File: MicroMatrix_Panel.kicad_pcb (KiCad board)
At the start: 2 copper layers, 86 x 36 mm, 321 parts

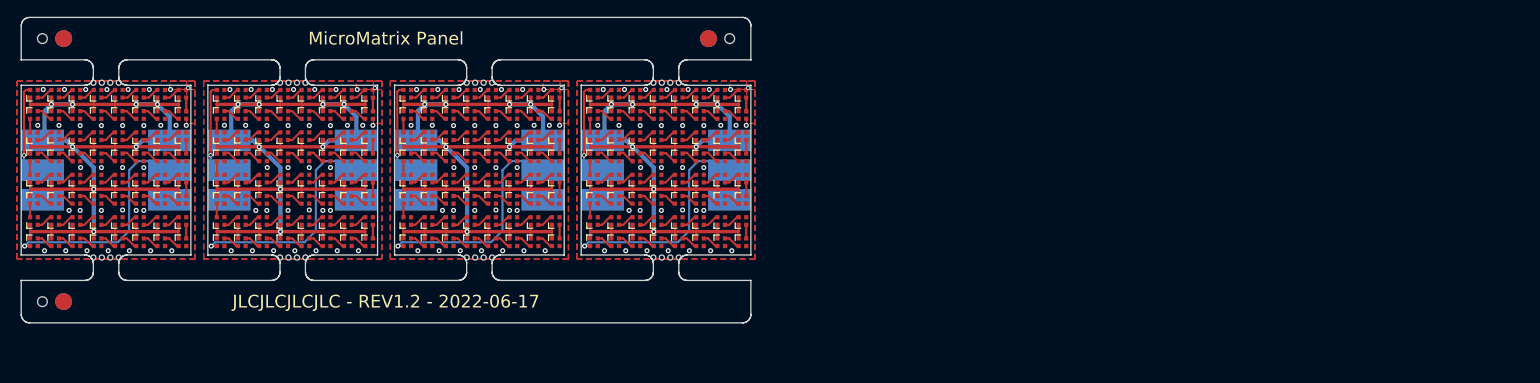
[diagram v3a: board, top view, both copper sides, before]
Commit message: Updated PCB to REV1.3 Replaced SK6805 footprint/symbol with a own version
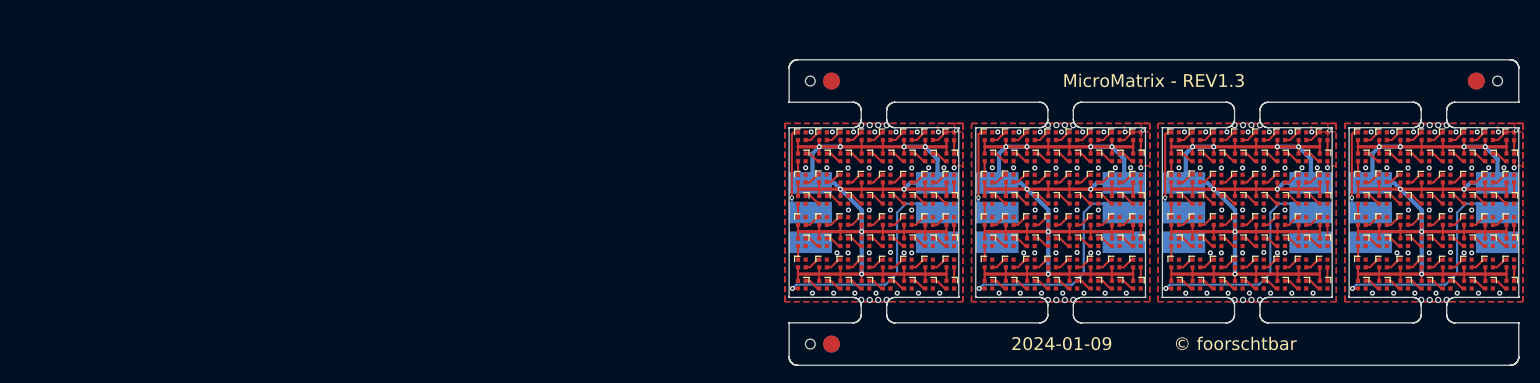
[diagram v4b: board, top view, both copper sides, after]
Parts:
- removed the ? at (39.5, 33.0)
- removed the ? at (17.5, 33.0)
- removed the ? at (83.5, 33.0)
- removed the ? at (39.5, 36.5)
- removed the ? at (76.5, 36.5)
- removed the ? at (17.5, 28.2)
- removed the ? at (17.5, 36.5)
- removed the ? at (98.5, 36.5)
- removed the ? at (98.5, 33.0)
- removed the ? at (32.5, 33.0)
- removed the ? at (61.5, 36.5)
- removed the ? at (54.5, 36.5)
- removed the ? at (54.5, 29.5)
- removed the ? at (54.5, 33.0)
- removed the ? at (83.5, 36.5)
- removed the ? at (61.5, 33.0)
- removed the ? at (98.5, 29.5)
- removed the ? at (32.5, 29.5)
- removed the ? at (61.5, 28.2)
- removed the ? at (76.5, 29.5)
- removed the ? at (39.5, 28.2)
- removed the ? at (76.5, 33.0)
- removed the ? at (83.5, 28.2)
- removed the ? at (32.5, 36.5)
- removed the D1 at (60.5, 24.0)
- removed the D1 at (16.5, 24.0)
- removed the D1 at (82.5, 24.0)
- removed the D1 at (38.5, 24.0)
- removed the D10 at (53.5, 26.5)
- removed the D10 at (31.5, 26.5)
- removed the D10 at (75.5, 26.5)
- removed the D10 at (97.5, 26.5)
- removed the D11 at (29.0, 26.5)
- removed the D11 at (73.0, 26.5)
- removed the D11 at (51.0, 26.5)
- removed the D11 at (95.0, 26.5)
- removed the D12 at (70.5, 26.5)
- removed the D12 at (92.5, 26.5)
- removed the D12 at (48.5, 26.5)
- removed the D12 at (26.5, 26.5)
- removed the D13 at (46.0, 26.5)
- removed the D13 at (24.0, 26.5)
- removed the D13 at (68.0, 26.5)
- removed the D13 at (90.0, 26.5)
- removed the D14 at (87.5, 26.5)
- removed the D14 at (43.5, 26.5)
- removed the D14 at (65.5, 26.5)
- removed the D14 at (21.5, 26.5)
- removed the D15 at (63.0, 26.5)
- removed the D15 at (19.0, 26.5)
- removed the D15 at (85.0, 26.5)
- removed the D15 at (41.0, 26.5)
- removed the D16 at (60.5, 26.5)
- removed the D16 at (82.5, 26.5)
- removed the D16 at (38.5, 26.5)
- removed the D16 at (16.5, 26.5)
- removed the D17 at (60.5, 29.0)
- removed the D17 at (16.5, 29.0)
- removed the D17 at (38.5, 29.0)
- removed the D17 at (82.5, 29.0)
- removed the D18 at (41.0, 28.9)
- removed the D18 at (63.0, 28.9)
- removed the D18 at (85.0, 28.9)
- removed the D18 at (19.0, 28.9)
- removed the D19 at (87.5, 29.0)
- removed the D19 at (43.5, 29.0)
- removed the D19 at (65.5, 29.0)
- removed the D19 at (21.5, 29.0)
- removed the D2 at (63.0, 24.0)
- removed the D2 at (85.0, 24.0)
- removed the D2 at (41.0, 24.0)
- removed the D2 at (19.0, 24.0)
- removed the D20 at (24.0, 29.0)
- removed the D20 at (46.0, 29.0)
- removed the D20 at (90.0, 29.0)
- removed the D20 at (68.0, 29.0)
- removed the D21 at (70.5, 29.0)
- removed the D21 at (48.5, 29.0)
- removed the D21 at (92.5, 29.0)
- removed the D21 at (26.5, 29.0)
- removed the D22 at (95.0, 29.0)
- removed the D22 at (29.0, 29.0)
- removed the D22 at (51.0, 29.0)
- removed the D22 at (73.0, 29.0)
- removed the D23 at (31.5, 29.0)
- removed the D23 at (53.5, 29.0)
- removed the D23 at (97.5, 29.0)
- removed the D23 at (75.5, 29.0)
- removed the D24 at (34.0, 29.0)
- removed the D24 at (56.0, 29.0)
- removed the D24 at (78.0, 29.0)
- removed the D24 at (100.0, 29.0)
- removed the D25 at (56.0, 31.5)
- removed the D25 at (78.0, 31.5)
- removed the D25 at (34.0, 31.5)
- removed the D25 at (100.0, 31.5)
- removed the D26 at (97.5, 31.5)
- removed the D26 at (75.5, 31.5)
- removed the D26 at (31.5, 31.5)
- removed the D26 at (53.5, 31.5)
- removed the D27 at (29.0, 31.5)
- removed the D27 at (73.0, 31.5)
- removed the D27 at (51.0, 31.5)
- removed the D27 at (95.0, 31.5)
- removed the D28 at (92.5, 31.5)
- removed the D28 at (70.5, 31.5)
- removed the D28 at (26.5, 31.5)
- removed the D28 at (48.5, 31.5)
- removed the D29 at (46.0, 31.5)
- removed the D29 at (90.0, 31.5)
- removed the D29 at (68.0, 31.5)
- removed the D29 at (24.0, 31.5)
- removed the D3 at (87.5, 24.0)
- removed the D3 at (43.5, 24.0)
- removed the D3 at (21.5, 24.0)
- removed the D3 at (65.5, 24.0)
- removed the D30 at (87.5, 31.5)
- removed the D30 at (65.5, 31.5)
- removed the D30 at (21.5, 31.5)
- removed the D30 at (43.5, 31.5)
- removed the D31 at (63.0, 31.5)
- removed the D31 at (85.0, 31.5)
- removed the D31 at (41.0, 31.5)
- removed the D31 at (19.0, 31.5)
- removed the D32 at (60.5, 31.5)
- removed the D32 at (38.5, 31.5)
- removed the D32 at (16.5, 31.5)
- removed the D32 at (82.5, 31.5)
- removed the D33 at (38.5, 34.0)
- removed the D33 at (82.5, 34.0)
- removed the D33 at (16.5, 34.0)
- removed the D33 at (60.5, 34.0)
- removed the D34 at (85.0, 34.0)
- removed the D34 at (19.0, 34.0)
- removed the D34 at (63.0, 34.0)
- removed the D34 at (41.0, 34.0)
- removed the D35 at (21.5, 34.0)
- removed the D35 at (43.5, 34.0)
- removed the D35 at (65.5, 34.0)
- removed the D35 at (87.5, 34.0)
- removed the D36 at (68.0, 34.0)
- removed the D36 at (46.0, 34.0)
- removed the D36 at (90.0, 34.0)
- removed the D36 at (24.0, 34.0)
- removed the D37 at (70.5, 34.0)
- removed the D37 at (92.5, 34.0)
- removed the D37 at (26.5, 34.0)
- removed the D37 at (48.5, 34.0)
- removed the D38 at (73.0, 34.0)
- removed the D38 at (95.0, 34.0)
- removed the D38 at (29.0, 34.0)
- removed the D38 at (51.0, 34.0)
- removed the D39 at (75.5, 34.0)
- removed the D39 at (31.5, 34.0)
- removed the D39 at (53.5, 34.0)
- removed the D39 at (97.5, 34.0)
- removed the D4 at (68.0, 24.0)
- removed the D4 at (90.0, 24.0)
- removed the D4 at (24.0, 24.0)
- removed the D4 at (46.0, 24.0)
- removed the D40 at (78.0, 34.0)
- removed the D40 at (34.0, 34.0)
- removed the D40 at (100.0, 34.0)
- removed the D40 at (56.0, 34.0)
- removed the D41 at (78.0, 36.5)
- removed the D41 at (100.0, 36.5)
- removed the D41 at (56.0, 36.5)
- removed the D41 at (34.0, 36.5)
- removed the D42 at (75.5, 36.5)
- removed the D42 at (97.5, 36.5)
- removed the D42 at (31.5, 36.5)
- removed the D42 at (53.5, 36.5)
- removed the D43 at (73.0, 36.5)
- removed the D43 at (29.0, 36.5)
- removed the D43 at (95.0, 36.5)
- removed the D43 at (51.0, 36.5)
- removed the D44 at (26.5, 36.5)
- removed the D44 at (92.5, 36.5)
- removed the D44 at (70.5, 36.5)
- removed the D44 at (48.5, 36.5)
- removed the D45 at (46.0, 36.5)
- removed the D45 at (68.0, 36.5)
- removed the D45 at (90.0, 36.5)
- removed the D45 at (24.0, 36.5)
- removed the D46 at (65.5, 36.5)
- removed the D46 at (43.5, 36.5)
- removed the D46 at (87.5, 36.5)
- removed the D46 at (21.5, 36.5)
- removed the D47 at (63.0, 36.5)
- removed the D47 at (19.0, 36.5)
- removed the D47 at (41.0, 36.5)
- removed the D47 at (85.0, 36.5)
- removed the D48 at (16.5, 36.5)
- removed the D48 at (38.5, 36.5)
- removed the D48 at (60.5, 36.5)
- removed the D48 at (82.5, 36.5)
- removed the D49 at (38.5, 39.0)
- removed the D49 at (16.5, 39.0)
- removed the D49 at (82.5, 39.0)
- removed the D49 at (60.5, 39.0)
- removed the D5 at (70.5, 24.0)
- removed the D5 at (26.5, 24.0)
- removed the D5 at (48.5, 24.0)
- removed the D5 at (92.5, 24.0)
- removed the D50 at (63.0, 39.0)
- removed the D50 at (19.0, 39.0)
- removed the D50 at (85.0, 39.0)
- removed the D50 at (41.0, 39.0)
- removed the D51 at (21.5, 39.0)
- removed the D51 at (65.5, 39.0)
- removed the D51 at (87.5, 39.0)
- removed the D51 at (43.5, 39.0)
- removed the D52 at (24.0, 39.0)
- removed the D52 at (46.0, 39.0)
- removed the D52 at (68.0, 39.0)
- removed the D52 at (90.0, 39.0)
- removed the D53 at (48.5, 39.0)
- removed the D53 at (70.5, 39.0)
- removed the D53 at (26.5, 39.0)
- removed the D53 at (92.5, 39.0)
- removed the D54 at (73.0, 39.0)
- removed the D54 at (95.0, 39.0)
- removed the D54 at (51.0, 39.0)
- removed the D54 at (29.0, 39.0)
- removed the D55 at (53.5, 39.0)
- removed the D55 at (97.5, 39.0)
- removed the D55 at (75.5, 39.0)
- removed the D55 at (31.5, 39.0)
- removed the D56 at (34.0, 39.0)
- removed the D56 at (100.0, 39.0)
- removed the D56 at (78.0, 39.0)
- removed the D56 at (56.0, 39.0)
- removed the D57 at (34.0, 41.5)
- removed the D57 at (78.0, 41.5)
- removed the D57 at (100.0, 41.5)
- removed the D57 at (56.0, 41.5)
- removed the D58 at (31.5, 41.5)
- removed the D58 at (53.5, 41.5)
- removed the D58 at (97.5, 41.5)
- removed the D58 at (75.5, 41.5)
- removed the D59 at (51.0, 41.5)
- removed the D59 at (95.0, 41.5)
- removed the D59 at (29.0, 41.5)
- removed the D59 at (73.0, 41.5)
- removed the D6 at (95.0, 24.0)
- removed the D6 at (51.0, 24.0)
- removed the D6 at (29.0, 24.0)
- removed the D6 at (73.0, 24.0)
- removed the D60 at (92.5, 41.5)
- removed the D60 at (70.5, 41.5)
- removed the D60 at (48.5, 41.5)
- removed the D60 at (26.5, 41.5)
- removed the D61 at (46.0, 41.5)
- removed the D61 at (24.0, 41.5)
- removed the D61 at (68.0, 41.5)
- removed the D61 at (90.0, 41.5)
- removed the D62 at (43.5, 41.5)
- removed the D62 at (65.5, 41.5)
- removed the D62 at (87.5, 41.5)
- removed the D62 at (21.5, 41.5)
- removed the D63 at (41.0, 41.5)
- removed the D63 at (85.0, 41.5)
- removed the D63 at (63.0, 41.5)
- removed the D63 at (19.0, 41.5)
- removed the D64 at (16.5, 41.5)
- removed the D64 at (60.5, 41.5)
- removed the D64 at (82.5, 41.5)
- removed the D64 at (38.5, 41.5)
- removed the D7 at (31.5, 24.0)
- removed the D7 at (75.5, 24.0)
- removed the D7 at (97.5, 24.0)
- removed the D7 at (53.5, 24.0)
- removed the D8 at (34.0, 24.0)
- removed the D8 at (100.0, 24.0)
- removed the D8 at (78.0, 24.0)
- removed the D8 at (56.0, 24.0)
- removed the D9 at (34.0, 26.5)
- removed the D9 at (100.0, 26.5)
- removed the D9 at (56.0, 26.5)
- removed the D9 at (78.0, 26.5)
- removed the REF** at (17.5, 17.5)
- removed the REF** at (67.5, 22.7)
- removed the REF** at (67.5, 43.3)
- removed the REF** at (47.5, 22.7)
- removed the REF** at (24.5, 22.7)
- removed the REF** at (20.0, 17.5) (x2)
- removed the REF** at (45.5, 22.7)
- removed the REF** at (90.5, 43.3)
- removed the REF** at (48.5, 43.3)
- removed the REF** at (70.5, 22.7)
- removed the REF** at (69.5, 43.3)
- removed the REF** at (26.5, 22.7)
- removed the REF** at (96.0, 17.5) (x2)
- removed the REF** at (98.5, 17.5)
- removed the REF** at (47.5, 43.3)
- removed the REF** at (23.5, 43.3)
- removed the REF** at (25.5, 43.3)
- removed the REF** at (89.5, 22.7)
- removed the REF** at (68.5, 43.3)
- removed the REF** at (24.5, 43.3)
- removed the REF** at (25.5, 22.7)
- removed the REF** at (46.5, 22.7)
- removed the REF** at (48.5, 22.7)
- removed the REF** at (91.5, 22.7)
- removed the REF** at (45.5, 43.3)
- removed the REF** at (17.5, 48.5)
- removed the REF** at (91.5, 43.3)
- removed the REF** at (20.0, 48.5) (x2)
- removed the REF** at (23.5, 22.7)
- removed the REF** at (68.5, 22.7)
- removed the REF** at (26.5, 43.3)
- removed the REF** at (70.5, 43.3)
- removed the REF** at (89.5, 43.3)
- removed the REF** at (92.5, 43.3)
- removed the REF** at (90.5, 22.7)
- removed the REF** at (92.5, 22.7)
- removed the REF** at (69.5, 22.7)
- removed the REF** at (46.5, 43.3)
- added ?: , , F.Cu at (152.0, 41.5)
- added ?: , , F.Cu at (145.0, 41.5)
- added ?: , , F.Cu at (174.0, 38.0)
- added ?: , , F.Cu at (108.0, 38.0)
- added ?: , , F.Cu at (123.0, 38.0)
- added ?: , , F.Cu at (130.0, 38.0)
- added ?: , , F.Cu at (167.0, 34.5)
- added ?: , , F.Cu at (189.0, 34.5)
- added ?: , , F.Cu at (108.0, 33.2)
- added ?: , , F.Cu at (145.0, 38.0)
- added ?: , , F.Cu at (152.0, 33.2)
- added ?: , , F.Cu at (130.0, 41.5)
- added ?: , , F.Cu at (189.0, 41.5)
- added ?: , , F.Cu at (123.0, 41.5)
- added ?: , , F.Cu at (189.0, 38.0)
- added ?: , , F.Cu at (152.0, 38.0)
- added ?: , , F.Cu at (145.0, 34.5)
- added ?: , , F.Cu at (174.0, 33.2)
- added ?: , , F.Cu at (130.0, 33.2)
- added ?: , , F.Cu at (167.0, 38.0)
- added ?: , , F.Cu at (174.0, 41.5)
- added ?: , , F.Cu at (167.0, 41.5)
- added ?: , , F.Cu at (108.0, 41.5)
- added ?: , , F.Cu at (123.0, 34.5)
- added D1: SK6805, SK6805-EC15:SK6805-EC15, F.Cu at (129.0, 29.0)
- added D1: SK6805, SK6805-EC15:SK6805-EC15, F.Cu at (151.0, 29.0)
- added D1: SK6805, SK6805-EC15:SK6805-EC15, F.Cu at (173.0, 29.0)
- added D1: SK6805, SK6805-EC15:SK6805-EC15, F.Cu at (107.0, 29.0)
- added D10: SK6805, SK6805-EC15:SK6805-EC15, F.Cu at (166.0, 31.5)
- added D10: SK6805, SK6805-EC15:SK6805-EC15, F.Cu at (188.0, 31.5)
- added D10: SK6805, SK6805-EC15:SK6805-EC15, F.Cu at (122.0, 31.5)
- added D10: SK6805, SK6805-EC15:SK6805-EC15, F.Cu at (144.0, 31.5)
- added D11: SK6805, SK6805-EC15:SK6805-EC15, F.Cu at (185.5, 31.5)
- added D11: SK6805, SK6805-EC15:SK6805-EC15, F.Cu at (119.5, 31.5)
- added D11: SK6805, SK6805-EC15:SK6805-EC15, F.Cu at (163.5, 31.5)
- added D11: SK6805, SK6805-EC15:SK6805-EC15, F.Cu at (141.5, 31.5)
- added D12: SK6805, SK6805-EC15:SK6805-EC15, F.Cu at (161.0, 31.5)
- added D12: SK6805, SK6805-EC15:SK6805-EC15, F.Cu at (117.0, 31.5)
- added D12: SK6805, SK6805-EC15:SK6805-EC15, F.Cu at (139.0, 31.5)
- added D12: SK6805, SK6805-EC15:SK6805-EC15, F.Cu at (183.0, 31.5)
- added D13: SK6805, SK6805-EC15:SK6805-EC15, F.Cu at (136.5, 31.5)
- added D13: SK6805, SK6805-EC15:SK6805-EC15, F.Cu at (114.5, 31.5)
- added D13: SK6805, SK6805-EC15:SK6805-EC15, F.Cu at (158.5, 31.5)
- added D13: SK6805, SK6805-EC15:SK6805-EC15, F.Cu at (180.5, 31.5)
- added D14: SK6805, SK6805-EC15:SK6805-EC15, F.Cu at (156.0, 31.5)
- added D14: SK6805, SK6805-EC15:SK6805-EC15, F.Cu at (134.0, 31.5)
- added D14: SK6805, SK6805-EC15:SK6805-EC15, F.Cu at (178.0, 31.5)
- added D14: SK6805, SK6805-EC15:SK6805-EC15, F.Cu at (112.0, 31.5)
- added D15: SK6805, SK6805-EC15:SK6805-EC15, F.Cu at (153.5, 31.5)
- added D15: SK6805, SK6805-EC15:SK6805-EC15, F.Cu at (109.5, 31.5)
- added D15: SK6805, SK6805-EC15:SK6805-EC15, F.Cu at (131.5, 31.5)
- added D15: SK6805, SK6805-EC15:SK6805-EC15, F.Cu at (175.5, 31.5)
- added D16: SK6805, SK6805-EC15:SK6805-EC15, F.Cu at (107.0, 31.5)
- added D16: SK6805, SK6805-EC15:SK6805-EC15, F.Cu at (151.0, 31.5)
- added D16: SK6805, SK6805-EC15:SK6805-EC15, F.Cu at (129.0, 31.5)
- added D16: SK6805, SK6805-EC15:SK6805-EC15, F.Cu at (173.0, 31.5)
- added D17: SK6805, SK6805-EC15:SK6805-EC15, F.Cu at (173.0, 34.0)
- added D17: SK6805, SK6805-EC15:SK6805-EC15, F.Cu at (129.0, 34.0)
- added D17: SK6805, SK6805-EC15:SK6805-EC15, F.Cu at (151.0, 34.0)
- added D17: SK6805, SK6805-EC15:SK6805-EC15, F.Cu at (107.0, 34.0)
- added D18: SK6805, SK6805-EC15:SK6805-EC15, F.Cu at (153.5, 34.0)
- added D18: SK6805, SK6805-EC15:SK6805-EC15, F.Cu at (175.5, 34.0)
- added D18: SK6805, SK6805-EC15:SK6805-EC15, F.Cu at (109.5, 34.0)
- added D18: SK6805, SK6805-EC15:SK6805-EC15, F.Cu at (131.5, 34.0)
- added D19: SK6805, SK6805-EC15:SK6805-EC15, F.Cu at (134.0, 34.0)
- added D19: SK6805, SK6805-EC15:SK6805-EC15, F.Cu at (178.0, 34.0)
- added D19: SK6805, SK6805-EC15:SK6805-EC15, F.Cu at (112.0, 34.0)
- added D19: SK6805, SK6805-EC15:SK6805-EC15, F.Cu at (156.0, 34.0)
- added D2: SK6805, SK6805-EC15:SK6805-EC15, F.Cu at (131.5, 29.0)
- added D2: SK6805, SK6805-EC15:SK6805-EC15, F.Cu at (153.5, 29.0)
- added D2: SK6805, SK6805-EC15:SK6805-EC15, F.Cu at (175.5, 29.0)
- added D2: SK6805, SK6805-EC15:SK6805-EC15, F.Cu at (109.5, 29.0)
- added D20: SK6805, SK6805-EC15:SK6805-EC15, F.Cu at (136.5, 34.0)
- added D20: SK6805, SK6805-EC15:SK6805-EC15, F.Cu at (114.5, 34.0)
- added D20: SK6805, SK6805-EC15:SK6805-EC15, F.Cu at (180.5, 34.0)
- added D20: SK6805, SK6805-EC15:SK6805-EC15, F.Cu at (158.5, 34.0)
- added D21: SK6805, SK6805-EC15:SK6805-EC15, F.Cu at (139.0, 34.0)
- added D21: SK6805, SK6805-EC15:SK6805-EC15, F.Cu at (183.0, 34.0)
- added D21: SK6805, SK6805-EC15:SK6805-EC15, F.Cu at (161.0, 34.0)
- added D21: SK6805, SK6805-EC15:SK6805-EC15, F.Cu at (117.0, 34.0)
- added D22: SK6805, SK6805-EC15:SK6805-EC15, F.Cu at (119.5, 34.0)
- added D22: SK6805, SK6805-EC15:SK6805-EC15, F.Cu at (163.5, 34.0)
- added D22: SK6805, SK6805-EC15:SK6805-EC15, F.Cu at (185.5, 34.0)
- added D22: SK6805, SK6805-EC15:SK6805-EC15, F.Cu at (141.5, 34.0)
- added D23: SK6805, SK6805-EC15:SK6805-EC15, F.Cu at (122.0, 34.0)
- added D23: SK6805, SK6805-EC15:SK6805-EC15, F.Cu at (144.0, 34.0)
- added D23: SK6805, SK6805-EC15:SK6805-EC15, F.Cu at (188.0, 34.0)
- added D23: SK6805, SK6805-EC15:SK6805-EC15, F.Cu at (166.0, 34.0)
- added D24: SK6805, SK6805-EC15:SK6805-EC15, F.Cu at (190.5, 34.0)
- added D24: SK6805, SK6805-EC15:SK6805-EC15, F.Cu at (124.5, 34.0)
- added D24: SK6805, SK6805-EC15:SK6805-EC15, F.Cu at (146.5, 34.0)
- added D24: SK6805, SK6805-EC15:SK6805-EC15, F.Cu at (168.5, 34.0)
- added D25: SK6805, SK6805-EC15:SK6805-EC15, F.Cu at (146.5, 36.5)
- added D25: SK6805, SK6805-EC15:SK6805-EC15, F.Cu at (190.5, 36.5)
- added D25: SK6805, SK6805-EC15:SK6805-EC15, F.Cu at (168.5, 36.5)
- added D25: SK6805, SK6805-EC15:SK6805-EC15, F.Cu at (124.5, 36.5)
- added D26: SK6805, SK6805-EC15:SK6805-EC15, F.Cu at (122.0, 36.5)
- added D26: SK6805, SK6805-EC15:SK6805-EC15, F.Cu at (144.0, 36.5)
- added D26: SK6805, SK6805-EC15:SK6805-EC15, F.Cu at (166.0, 36.5)
- added D26: SK6805, SK6805-EC15:SK6805-EC15, F.Cu at (188.0, 36.5)
- added D27: SK6805, SK6805-EC15:SK6805-EC15, F.Cu at (185.5, 36.5)
- added D27: SK6805, SK6805-EC15:SK6805-EC15, F.Cu at (141.5, 36.5)
- added D27: SK6805, SK6805-EC15:SK6805-EC15, F.Cu at (163.5, 36.5)
- added D27: SK6805, SK6805-EC15:SK6805-EC15, F.Cu at (119.5, 36.5)
- added D28: SK6805, SK6805-EC15:SK6805-EC15, F.Cu at (117.0, 36.5)
- added D28: SK6805, SK6805-EC15:SK6805-EC15, F.Cu at (139.0, 36.5)
- added D28: SK6805, SK6805-EC15:SK6805-EC15, F.Cu at (183.0, 36.5)
- added D28: SK6805, SK6805-EC15:SK6805-EC15, F.Cu at (161.0, 36.5)
- added D29: SK6805, SK6805-EC15:SK6805-EC15, F.Cu at (114.5, 36.5)
- added D29: SK6805, SK6805-EC15:SK6805-EC15, F.Cu at (180.5, 36.5)
- added D29: SK6805, SK6805-EC15:SK6805-EC15, F.Cu at (158.5, 36.5)
- added D29: SK6805, SK6805-EC15:SK6805-EC15, F.Cu at (136.5, 36.5)
- added D3: SK6805, SK6805-EC15:SK6805-EC15, F.Cu at (112.0, 29.0)
- added D3: SK6805, SK6805-EC15:SK6805-EC15, F.Cu at (156.0, 29.0)
- added D3: SK6805, SK6805-EC15:SK6805-EC15, F.Cu at (134.0, 29.0)
- added D3: SK6805, SK6805-EC15:SK6805-EC15, F.Cu at (178.0, 29.0)
- added D30: SK6805, SK6805-EC15:SK6805-EC15, F.Cu at (112.0, 36.5)
- added D30: SK6805, SK6805-EC15:SK6805-EC15, F.Cu at (178.0, 36.5)
- added D30: SK6805, SK6805-EC15:SK6805-EC15, F.Cu at (134.0, 36.5)
- added D30: SK6805, SK6805-EC15:SK6805-EC15, F.Cu at (156.0, 36.5)
- added D31: SK6805, SK6805-EC15:SK6805-EC15, F.Cu at (175.5, 36.5)
- added D31: SK6805, SK6805-EC15:SK6805-EC15, F.Cu at (131.5, 36.5)
- added D31: SK6805, SK6805-EC15:SK6805-EC15, F.Cu at (153.5, 36.5)
- added D31: SK6805, SK6805-EC15:SK6805-EC15, F.Cu at (109.5, 36.5)
- added D32: SK6805, SK6805-EC15:SK6805-EC15, F.Cu at (151.0, 36.5)
- added D32: SK6805, SK6805-EC15:SK6805-EC15, F.Cu at (173.0, 36.5)
- added D32: SK6805, SK6805-EC15:SK6805-EC15, F.Cu at (107.0, 36.5)
- added D32: SK6805, SK6805-EC15:SK6805-EC15, F.Cu at (129.0, 36.5)
- added D33: SK6805, SK6805-EC15:SK6805-EC15, F.Cu at (173.0, 39.0)
- added D33: SK6805, SK6805-EC15:SK6805-EC15, F.Cu at (107.0, 39.0)
- added D33: SK6805, SK6805-EC15:SK6805-EC15, F.Cu at (151.0, 39.0)
- added D33: SK6805, SK6805-EC15:SK6805-EC15, F.Cu at (129.0, 39.0)
- added D34: SK6805, SK6805-EC15:SK6805-EC15, F.Cu at (175.5, 39.0)
- added D34: SK6805, SK6805-EC15:SK6805-EC15, F.Cu at (109.5, 39.0)
- added D34: SK6805, SK6805-EC15:SK6805-EC15, F.Cu at (131.5, 39.0)
- added D34: SK6805, SK6805-EC15:SK6805-EC15, F.Cu at (153.5, 39.0)
- added D35: SK6805, SK6805-EC15:SK6805-EC15, F.Cu at (134.0, 39.0)
- added D35: SK6805, SK6805-EC15:SK6805-EC15, F.Cu at (112.0, 39.0)
- added D35: SK6805, SK6805-EC15:SK6805-EC15, F.Cu at (156.0, 39.0)
- added D35: SK6805, SK6805-EC15:SK6805-EC15, F.Cu at (178.0, 39.0)
- added D36: SK6805, SK6805-EC15:SK6805-EC15, F.Cu at (114.5, 39.0)
- added D36: SK6805, SK6805-EC15:SK6805-EC15, F.Cu at (180.5, 39.0)
- added D36: SK6805, SK6805-EC15:SK6805-EC15, F.Cu at (136.5, 39.0)
- added D36: SK6805, SK6805-EC15:SK6805-EC15, F.Cu at (158.5, 39.0)
- added D37: SK6805, SK6805-EC15:SK6805-EC15, F.Cu at (161.0, 39.0)
- added D37: SK6805, SK6805-EC15:SK6805-EC15, F.Cu at (117.0, 39.0)
- added D37: SK6805, SK6805-EC15:SK6805-EC15, F.Cu at (183.0, 39.0)
- added D37: SK6805, SK6805-EC15:SK6805-EC15, F.Cu at (139.0, 39.0)
- added D38: SK6805, SK6805-EC15:SK6805-EC15, F.Cu at (141.5, 39.0)
- added D38: SK6805, SK6805-EC15:SK6805-EC15, F.Cu at (185.5, 39.0)
- added D38: SK6805, SK6805-EC15:SK6805-EC15, F.Cu at (119.5, 39.0)
- added D38: SK6805, SK6805-EC15:SK6805-EC15, F.Cu at (163.5, 39.0)
- added D39: SK6805, SK6805-EC15:SK6805-EC15, F.Cu at (166.0, 39.0)
- added D39: SK6805, SK6805-EC15:SK6805-EC15, F.Cu at (122.0, 39.0)
- added D39: SK6805, SK6805-EC15:SK6805-EC15, F.Cu at (144.0, 39.0)
- added D39: SK6805, SK6805-EC15:SK6805-EC15, F.Cu at (188.0, 39.0)
- added D4: SK6805, SK6805-EC15:SK6805-EC15, F.Cu at (180.5, 29.0)
- added D4: SK6805, SK6805-EC15:SK6805-EC15, F.Cu at (114.5, 29.0)
- added D4: SK6805, SK6805-EC15:SK6805-EC15, F.Cu at (136.5, 29.0)
- added D4: SK6805, SK6805-EC15:SK6805-EC15, F.Cu at (158.5, 29.0)
- added D40: SK6805, SK6805-EC15:SK6805-EC15, F.Cu at (124.5, 39.0)
- added D40: SK6805, SK6805-EC15:SK6805-EC15, F.Cu at (146.5, 39.0)
- added D40: SK6805, SK6805-EC15:SK6805-EC15, F.Cu at (168.5, 39.0)
- added D40: SK6805, SK6805-EC15:SK6805-EC15, F.Cu at (190.5, 39.0)
- added D41: SK6805, SK6805-EC15:SK6805-EC15, F.Cu at (168.5, 41.5)
- added D41: SK6805, SK6805-EC15:SK6805-EC15, F.Cu at (146.5, 41.5)
- added D41: SK6805, SK6805-EC15:SK6805-EC15, F.Cu at (190.5, 41.5)
- added D41: SK6805, SK6805-EC15:SK6805-EC15, F.Cu at (124.5, 41.5)
- added D42: SK6805, SK6805-EC15:SK6805-EC15, F.Cu at (122.0, 41.5)
- added D42: SK6805, SK6805-EC15:SK6805-EC15, F.Cu at (144.0, 41.5)
- added D42: SK6805, SK6805-EC15:SK6805-EC15, F.Cu at (166.0, 41.5)
- added D42: SK6805, SK6805-EC15:SK6805-EC15, F.Cu at (188.0, 41.5)
- added D43: SK6805, SK6805-EC15:SK6805-EC15, F.Cu at (119.5, 41.5)
- added D43: SK6805, SK6805-EC15:SK6805-EC15, F.Cu at (141.5, 41.5)
- added D43: SK6805, SK6805-EC15:SK6805-EC15, F.Cu at (185.5, 41.5)
- added D43: SK6805, SK6805-EC15:SK6805-EC15, F.Cu at (163.5, 41.5)
- added D44: SK6805, SK6805-EC15:SK6805-EC15, F.Cu at (183.0, 41.5)
- added D44: SK6805, SK6805-EC15:SK6805-EC15, F.Cu at (161.0, 41.5)
- added D44: SK6805, SK6805-EC15:SK6805-EC15, F.Cu at (139.0, 41.5)
- added D44: SK6805, SK6805-EC15:SK6805-EC15, F.Cu at (117.0, 41.5)
- added D45: SK6805, SK6805-EC15:SK6805-EC15, F.Cu at (136.5, 41.5)
- added D45: SK6805, SK6805-EC15:SK6805-EC15, F.Cu at (180.5, 41.5)
- added D45: SK6805, SK6805-EC15:SK6805-EC15, F.Cu at (158.5, 41.5)
- added D45: SK6805, SK6805-EC15:SK6805-EC15, F.Cu at (114.5, 41.5)
- added D46: SK6805, SK6805-EC15:SK6805-EC15, F.Cu at (178.0, 41.5)
- added D46: SK6805, SK6805-EC15:SK6805-EC15, F.Cu at (112.0, 41.5)
- added D46: SK6805, SK6805-EC15:SK6805-EC15, F.Cu at (134.0, 41.5)
- added D46: SK6805, SK6805-EC15:SK6805-EC15, F.Cu at (156.0, 41.5)
- added D47: SK6805, SK6805-EC15:SK6805-EC15, F.Cu at (109.5, 41.5)
- added D47: SK6805, SK6805-EC15:SK6805-EC15, F.Cu at (175.5, 41.5)
- added D47: SK6805, SK6805-EC15:SK6805-EC15, F.Cu at (153.5, 41.5)
- added D47: SK6805, SK6805-EC15:SK6805-EC15, F.Cu at (131.5, 41.5)
- added D48: SK6805, SK6805-EC15:SK6805-EC15, F.Cu at (129.0, 41.5)
- added D48: SK6805, SK6805-EC15:SK6805-EC15, F.Cu at (151.0, 41.5)
- added D48: SK6805, SK6805-EC15:SK6805-EC15, F.Cu at (107.0, 41.5)
- added D48: SK6805, SK6805-EC15:SK6805-EC15, F.Cu at (173.0, 41.5)
- added D49: SK6805, SK6805-EC15:SK6805-EC15, F.Cu at (107.0, 44.0)
- added D49: SK6805, SK6805-EC15:SK6805-EC15, F.Cu at (173.0, 44.0)
- added D49: SK6805, SK6805-EC15:SK6805-EC15, F.Cu at (129.0, 44.0)
- added D49: SK6805, SK6805-EC15:SK6805-EC15, F.Cu at (151.0, 44.0)
- added D5: SK6805, SK6805-EC15:SK6805-EC15, F.Cu at (139.0, 29.0)
- added D5: SK6805, SK6805-EC15:SK6805-EC15, F.Cu at (161.0, 29.0)
- added D5: SK6805, SK6805-EC15:SK6805-EC15, F.Cu at (117.0, 29.0)
- added D5: SK6805, SK6805-EC15:SK6805-EC15, F.Cu at (183.0, 29.0)
- added D50: SK6805, SK6805-EC15:SK6805-EC15, F.Cu at (153.5, 44.0)
- added D50: SK6805, SK6805-EC15:SK6805-EC15, F.Cu at (175.5, 44.0)
- added D50: SK6805, SK6805-EC15:SK6805-EC15, F.Cu at (131.5, 44.0)
- added D50: SK6805, SK6805-EC15:SK6805-EC15, F.Cu at (109.5, 44.0)
- added D51: SK6805, SK6805-EC15:SK6805-EC15, F.Cu at (112.0, 44.0)
- added D51: SK6805, SK6805-EC15:SK6805-EC15, F.Cu at (178.0, 44.0)
- added D51: SK6805, SK6805-EC15:SK6805-EC15, F.Cu at (134.0, 44.0)
- added D51: SK6805, SK6805-EC15:SK6805-EC15, F.Cu at (156.0, 44.0)
- added D52: SK6805, SK6805-EC15:SK6805-EC15, F.Cu at (158.5, 44.0)
- added D52: SK6805, SK6805-EC15:SK6805-EC15, F.Cu at (114.5, 44.0)
- added D52: SK6805, SK6805-EC15:SK6805-EC15, F.Cu at (180.5, 44.0)
- added D52: SK6805, SK6805-EC15:SK6805-EC15, F.Cu at (136.5, 44.0)
- added D53: SK6805, SK6805-EC15:SK6805-EC15, F.Cu at (139.0, 44.0)
- added D53: SK6805, SK6805-EC15:SK6805-EC15, F.Cu at (117.0, 44.0)
- added D53: SK6805, SK6805-EC15:SK6805-EC15, F.Cu at (183.0, 44.0)
- added D53: SK6805, SK6805-EC15:SK6805-EC15, F.Cu at (161.0, 44.0)
- added D54: SK6805, SK6805-EC15:SK6805-EC15, F.Cu at (163.5, 44.0)
- added D54: SK6805, SK6805-EC15:SK6805-EC15, F.Cu at (185.5, 44.0)
- added D54: SK6805, SK6805-EC15:SK6805-EC15, F.Cu at (119.5, 44.0)
- added D54: SK6805, SK6805-EC15:SK6805-EC15, F.Cu at (141.5, 44.0)
- added D55: SK6805, SK6805-EC15:SK6805-EC15, F.Cu at (144.0, 44.0)
- added D55: SK6805, SK6805-EC15:SK6805-EC15, F.Cu at (122.0, 44.0)
- added D55: SK6805, SK6805-EC15:SK6805-EC15, F.Cu at (188.0, 44.0)
- added D55: SK6805, SK6805-EC15:SK6805-EC15, F.Cu at (166.0, 44.0)
- added D56: SK6805, SK6805-EC15:SK6805-EC15, F.Cu at (124.5, 44.0)
- added D56: SK6805, SK6805-EC15:SK6805-EC15, F.Cu at (190.5, 44.0)
- added D56: SK6805, SK6805-EC15:SK6805-EC15, F.Cu at (168.5, 44.0)
- added D56: SK6805, SK6805-EC15:SK6805-EC15, F.Cu at (146.5, 44.0)
- added D57: SK6805, SK6805-EC15:SK6805-EC15, F.Cu at (146.5, 46.5)
- added D57: SK6805, SK6805-EC15:SK6805-EC15, F.Cu at (168.5, 46.5)
- added D57: SK6805, SK6805-EC15:SK6805-EC15, F.Cu at (190.5, 46.5)
- added D57: SK6805, SK6805-EC15:SK6805-EC15, F.Cu at (124.5, 46.5)
- added D58: SK6805, SK6805-EC15:SK6805-EC15, F.Cu at (166.0, 46.5)
- added D58: SK6805, SK6805-EC15:SK6805-EC15, F.Cu at (188.0, 46.5)
- added D58: SK6805, SK6805-EC15:SK6805-EC15, F.Cu at (122.0, 46.5)
- added D58: SK6805, SK6805-EC15:SK6805-EC15, F.Cu at (144.0, 46.5)
- added D59: SK6805, SK6805-EC15:SK6805-EC15, F.Cu at (163.5, 46.5)
- added D59: SK6805, SK6805-EC15:SK6805-EC15, F.Cu at (119.5, 46.5)
- added D59: SK6805, SK6805-EC15:SK6805-EC15, F.Cu at (141.5, 46.5)
- added D59: SK6805, SK6805-EC15:SK6805-EC15, F.Cu at (185.5, 46.5)
- added D6: SK6805, SK6805-EC15:SK6805-EC15, F.Cu at (185.5, 29.0)
- added D6: SK6805, SK6805-EC15:SK6805-EC15, F.Cu at (119.5, 29.0)
- added D6: SK6805, SK6805-EC15:SK6805-EC15, F.Cu at (163.5, 29.0)
- added D6: SK6805, SK6805-EC15:SK6805-EC15, F.Cu at (141.5, 29.0)
- added D60: SK6805, SK6805-EC15:SK6805-EC15, F.Cu at (161.0, 46.5)
- added D60: SK6805, SK6805-EC15:SK6805-EC15, F.Cu at (183.0, 46.5)
- added D60: SK6805, SK6805-EC15:SK6805-EC15, F.Cu at (139.0, 46.5)
- added D60: SK6805, SK6805-EC15:SK6805-EC15, F.Cu at (117.0, 46.5)
- added D61: SK6805, SK6805-EC15:SK6805-EC15, F.Cu at (136.5, 46.5)
- added D61: SK6805, SK6805-EC15:SK6805-EC15, F.Cu at (180.5, 46.5)
- added D61: SK6805, SK6805-EC15:SK6805-EC15, F.Cu at (114.5, 46.5)
- added D61: SK6805, SK6805-EC15:SK6805-EC15, F.Cu at (158.5, 46.5)
- added D62: SK6805, SK6805-EC15:SK6805-EC15, F.Cu at (134.0, 46.5)
- added D62: SK6805, SK6805-EC15:SK6805-EC15, F.Cu at (156.0, 46.5)
- added D62: SK6805, SK6805-EC15:SK6805-EC15, F.Cu at (178.0, 46.5)
- added D62: SK6805, SK6805-EC15:SK6805-EC15, F.Cu at (112.0, 46.5)
- added D63: SK6805, SK6805-EC15:SK6805-EC15, F.Cu at (109.5, 46.5)
- added D63: SK6805, SK6805-EC15:SK6805-EC15, F.Cu at (131.5, 46.5)
- added D63: SK6805, SK6805-EC15:SK6805-EC15, F.Cu at (153.5, 46.5)
- added D63: SK6805, SK6805-EC15:SK6805-EC15, F.Cu at (175.5, 46.5)
- added D64: SK6805, SK6805-EC15:SK6805-EC15, F.Cu at (151.0, 46.5)
- added D64: SK6805, SK6805-EC15:SK6805-EC15, F.Cu at (107.0, 46.5)
- added D64: SK6805, SK6805-EC15:SK6805-EC15, F.Cu at (173.0, 46.5)
- added D64: SK6805, SK6805-EC15:SK6805-EC15, F.Cu at (129.0, 46.5)
- added D7: SK6805, SK6805-EC15:SK6805-EC15, F.Cu at (188.0, 29.0)
- added D7: SK6805, SK6805-EC15:SK6805-EC15, F.Cu at (122.0, 29.0)
- added D7: SK6805, SK6805-EC15:SK6805-EC15, F.Cu at (166.0, 29.0)
- added D7: SK6805, SK6805-EC15:SK6805-EC15, F.Cu at (144.0, 29.0)
- added D8: SK6805, SK6805-EC15:SK6805-EC15, F.Cu at (190.5, 29.0)
- added D8: SK6805, SK6805-EC15:SK6805-EC15, F.Cu at (168.5, 29.0)
- added D8: SK6805, SK6805-EC15:SK6805-EC15, F.Cu at (146.5, 29.0)
- added D8: SK6805, SK6805-EC15:SK6805-EC15, F.Cu at (124.5, 29.0)
- added D9: SK6805, SK6805-EC15:SK6805-EC15, F.Cu at (190.5, 31.5)
- added D9: SK6805, SK6805-EC15:SK6805-EC15, F.Cu at (146.5, 31.5)
- added D9: SK6805, SK6805-EC15:SK6805-EC15, F.Cu at (168.5, 31.5)
- added D9: SK6805, SK6805-EC15:SK6805-EC15, F.Cu at (124.5, 31.5)
- added REF**: NPTH, NPTH, F.Cu at (159.0, 48.3)
- added REF**: NPTH, NPTH, F.Cu at (116.0, 48.3)
- added REF**: NPTH, NPTH, F.Cu at (158.0, 27.7)
- added REF**: NPTH, NPTH, F.Cu at (180.0, 48.3)
- added REF**: NPTH, NPTH, F.Cu at (183.0, 48.3)
- added REF**: NPTH, NPTH, F.Cu at (159.0, 27.7)
- added REF**: NPTH, NPTH, F.Cu at (116.0, 27.7)
- added REF**: NPTH, NPTH, F.Cu at (161.0, 48.3)
- added REF**: NPTH, NPTH, F.Cu at (183.0, 27.7)
- added REF**: NPTH, NPTH, F.Cu at (136.0, 48.3)
- added REF**: NPTH, NPTH, F.Cu at (114.0, 48.3)
- added REF**: NPTH, NPTH, F.Cu at (114.0, 27.7)
- added REF**: NPTH, NPTH, F.Cu at (182.0, 48.3)
- added REF**: NPTH, NPTH, F.Cu at (117.0, 48.3)
- added REF**: NPTH, NPTH, F.Cu at (161.0, 27.7)
- added REF**: NPTH, NPTH, F.Cu at (181.0, 48.3)
- added REF**: NPTH, NPTH, F.Cu at (108.0, 53.5)
- added REF**: NPTH, NPTH, F.Cu at (136.0, 27.7)
- added REF**: NPTH, NPTH, F.Cu at (115.0, 48.3)
- added REF**: NPTH, NPTH, F.Cu at (160.0, 48.3)
- added REF**: NPTH, NPTH, F.Cu at (160.0, 27.7)
- added REF**: NPTH, NPTH, F.Cu at (158.0, 48.3)
- added REF**: NPTH, NPTH, F.Cu at (182.0, 27.7)
- added REF**: NPTH, NPTH, F.Cu at (108.0, 22.5)
- added REF**: NPTH, NPTH, F.Cu at (139.0, 48.3)
- added REF**: Fiducial, Fiducial, F.Cu at (186.5, 22.5)
- added REF**: NPTH, NPTH, F.Cu at (138.0, 27.7)
- added REF**: NPTH, NPTH, F.Cu at (138.0, 48.3)
- added REF**: NPTH, NPTH, F.Cu at (137.0, 27.7)
- added REF**: NPTH, NPTH, F.Cu at (117.0, 27.7)
- added REF**: NPTH, NPTH, F.Cu at (139.0, 27.7)
- added REF**: NPTH, NPTH, F.Cu at (181.0, 27.7)
- added REF**: Fiducial, Fiducial, B.Cu at (186.5, 22.5)
- added REF**: NPTH, NPTH, F.Cu at (115.0, 27.7)
- added REF**: Fiducial, Fiducial, B.Cu at (110.5, 22.5)
- added REF**: Fiducial, Fiducial, B.Cu at (110.5, 53.5)
- added REF**: NPTH, NPTH, F.Cu at (137.0, 48.3)
- added REF**: NPTH, NPTH, F.Cu at (189.0, 22.5)
- added REF**: NPTH, NPTH, F.Cu at (180.0, 27.7)
- added REF**: Fiducial, Fiducial, F.Cu at (110.5, 53.5)
- added REF**: Fiducial, Fiducial, F.Cu at (110.5, 22.5)
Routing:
- net Board_3-Net-(D54-DOUT): track 0.00 -> 2.07 mm
- net Board_2-Net-(D54-DOUT): track 0.00 -> 2.07 mm
- net Board_1-Net-(D54-DOUT): track 0.00 -> 2.07 mm
- net Board_0-Net-(D54-Pad1): track 2.07 -> 0.00 mm
- net Board_1-Net-(D54-Pad1): track 2.07 -> 0.00 mm
- net Board_3-Net-(D54-Pad1): track 2.07 -> 0.00 mm
- net Board_2-Net-(D54-Pad1): track 2.07 -> 0.00 mm
- net Board_0-Net-(D54-DOUT): track 0.00 -> 2.07 mm
- net Board_3-Net-(D17-DOUT): track 0.00 -> 1.99 mm
- net Board_2-Net-(D17-DOUT): track 0.00 -> 1.99 mm
- net Board_1-Net-(D17-DOUT): track 0.00 -> 1.99 mm
- net Board_0-Net-(D17-Pad1): track 1.99 -> 0.00 mm
- net Board_0-Net-(D17-DOUT): track 0.00 -> 1.99 mm
- net Board_2-Net-(D17-Pad1): track 1.99 -> 0.00 mm
- net Board_1-Net-(D17-Pad1): track 1.99 -> 0.00 mm
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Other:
- outline, holes or cut-outs redrawn
- board text added: "${ISSUE_DATE} ${COMPANY}"
- board text added: "${TITLE} - REV${REVISION}"
- board text added: "2024/01"
- board text added: "JLCJLCJLCJLC"
- board text added: "REV1.3"
- board text removed: "${TITLE} Panel"
- board text removed: "2022/06"
- board text removed: "JLCJLCJLCJLC - REV${REVISION} - ${ISSUE_DATE}"
- board text removed: "REV1.2"
